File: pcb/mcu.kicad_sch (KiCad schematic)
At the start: 11 parts, among them SW1 TS-1088-AR02016, SW2 TS-1088-AR02016, U1 ESP32-S3-MINI-1

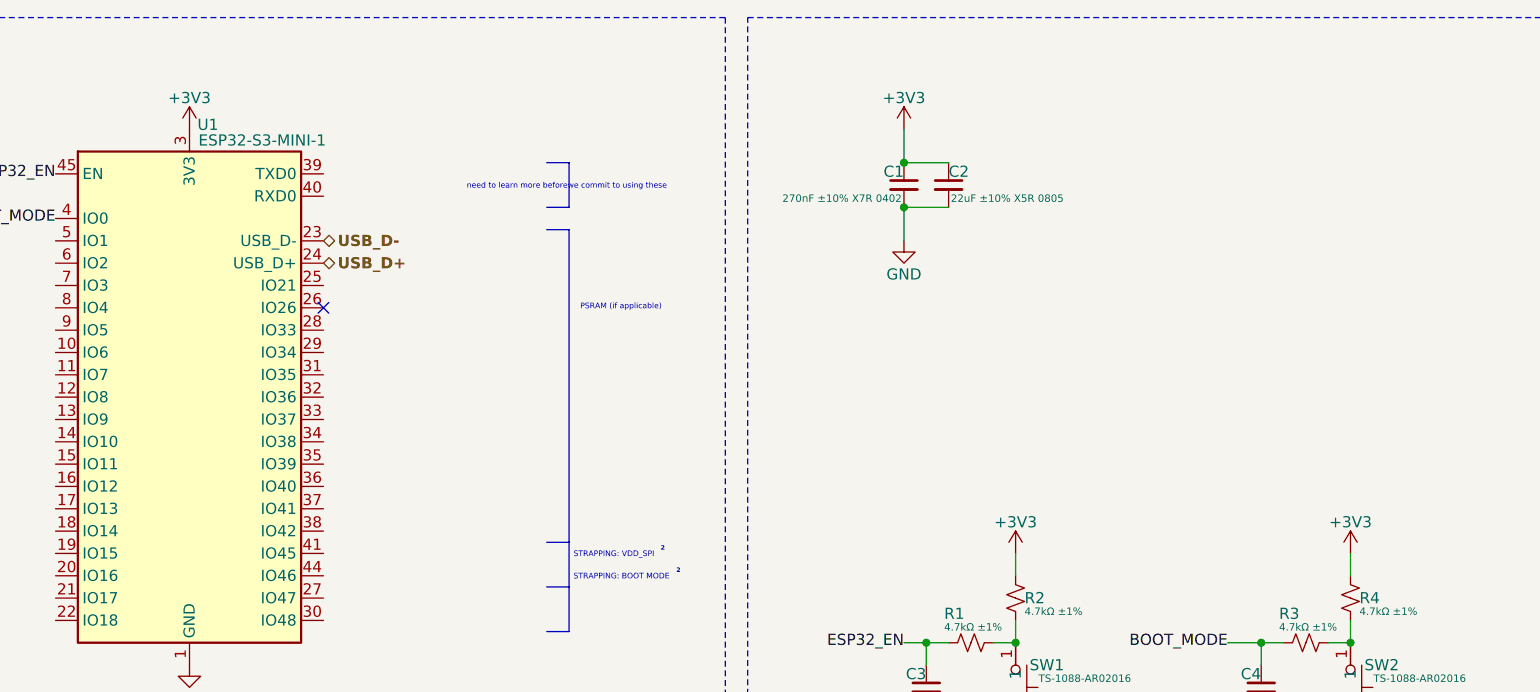
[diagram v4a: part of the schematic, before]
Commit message: Completed Initial Power Draft for Review, and Updated Flags
Included notes for review
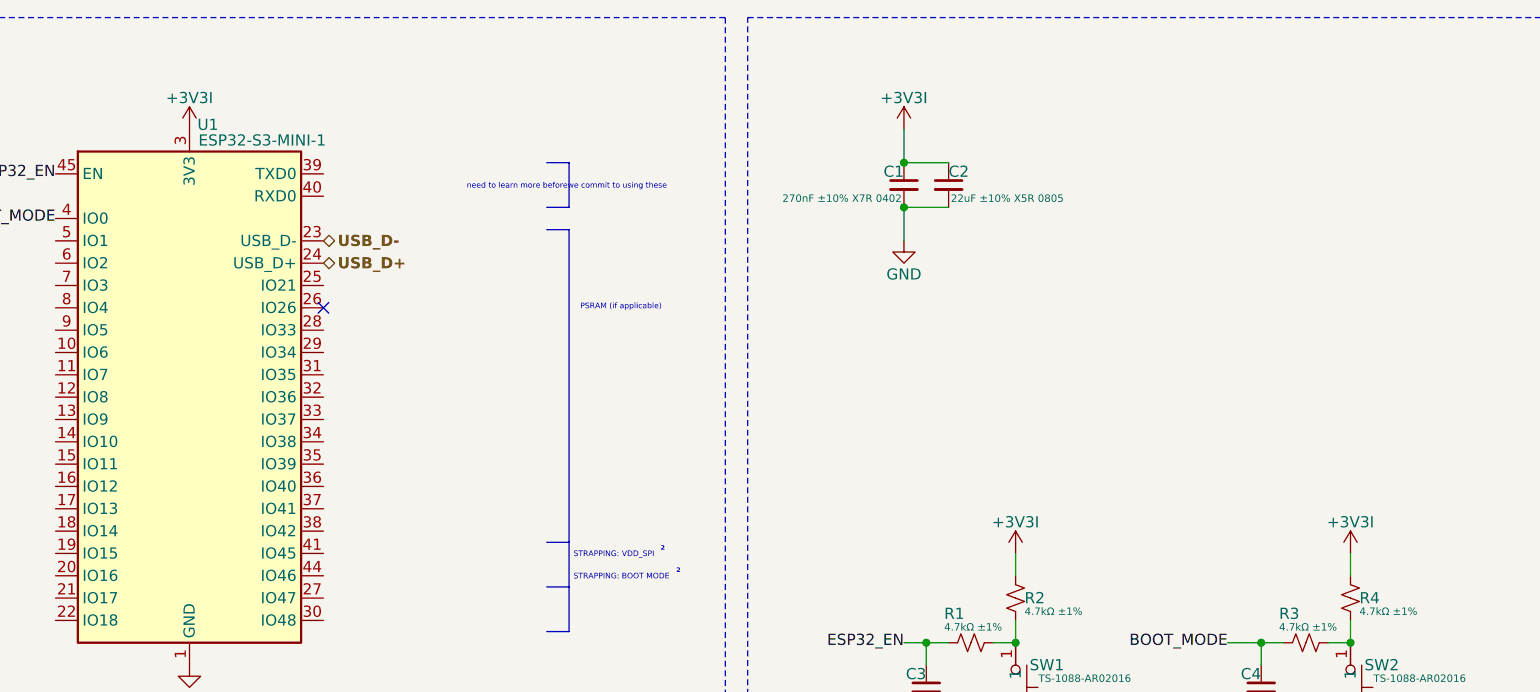
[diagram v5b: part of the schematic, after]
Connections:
- net +3V3 renamed +3V3I
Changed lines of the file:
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@@
 			)
 		)
-		(property "Value" "+3V3"
+		(property "Value" "+3V3I"
 			(at 208.28 70.104 0)
 			(effects
@@
 			)
 		)
-		(property "Value" "+3V3"
+		(property "Value" "+3V3I"
 			(at 246.38 70.104 0)
 			(effects
@@
 			)
 		)
-		(property "Value" "+3V3"
+		(property "Value" "+3V3I"
 			(at 195.58 21.844 0)
 			(effects
@@
 			)
 		)
-		(property "Value" "+3V3"
+		(property "Value" "+3V3I"
 			(at 114.3 21.844 0)
 			(effects

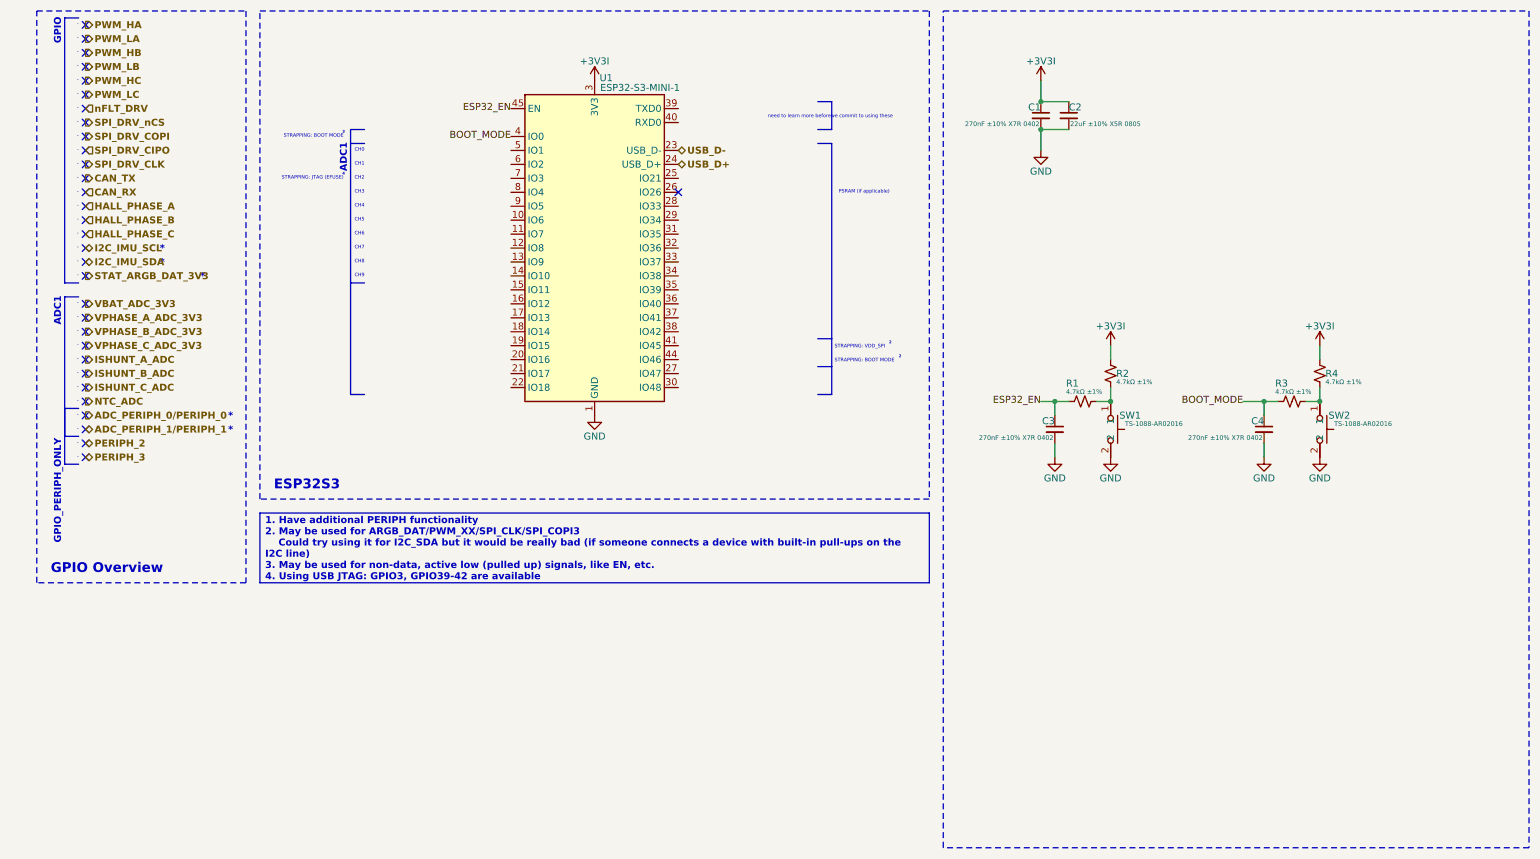
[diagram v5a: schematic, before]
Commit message: Updating label direction, added more info on io
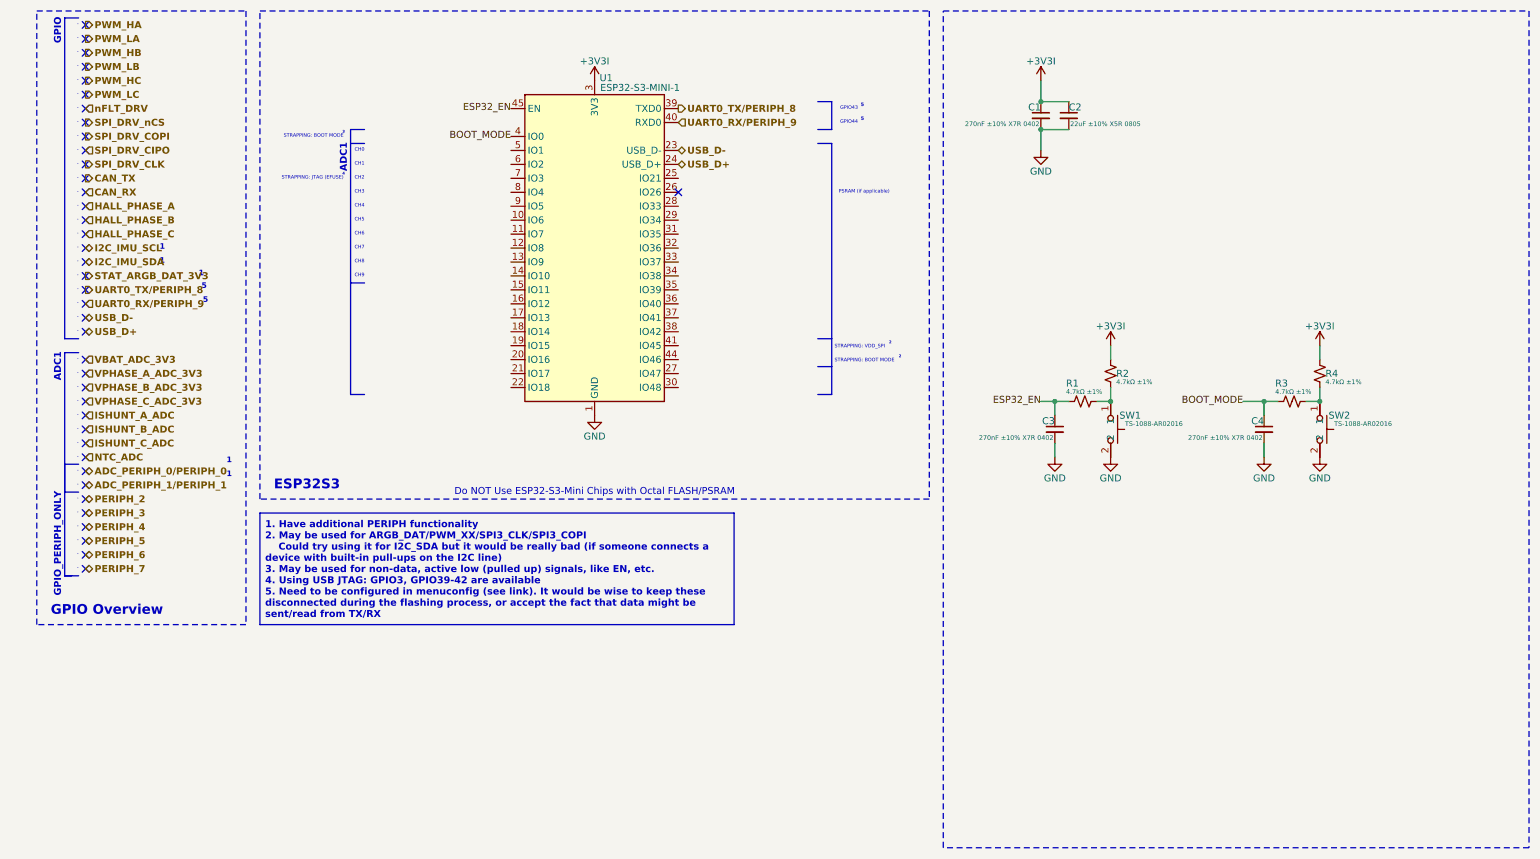
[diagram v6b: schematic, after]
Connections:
- net UART0_TX/PERIPH_8: now reaches U1.39 (TXD0)
- net UART0_RX/PERIPH_9: now reaches U1.40 (RXD0)
- no-connect marks 32 -> 40
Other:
- note added: "5"
- note added: "Do NOT Use ESP32-S3-Mini Chips with Octal FLASH/PSRAM"
- note added: "GPIO43"
- note added: "GPIO44"
- note added: "^{1}"
- note added: "^{5}"
- note removed: "*"
- note removed: "need to learn more beforewe commit to using these"

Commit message: Made updates to the power and driver sheet
Fixed converters and added motor connector
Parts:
- renumbered C2 to C?, C4 to C?, C1 to C?, C3 to C?, R1 to R?, R2 to R?, R3 to R?, R4 to R?, SW2 to SW?, SW1 to SW?, U1 to U?
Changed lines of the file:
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@@
 		(on_board yes)
 		(dnp no)
-		(property "Reference" "#PWR08"
+		(property "Reference" "#PWR?"
 			(at 236.22 100.33 0)
 			(effects
@@
 			(project "sresc"
 				(path "/5072676b-6ffc-4812-9165-a6d5aae17d98/1c391981-fffe-4c54-847d-b61b4420497c"
-					(reference "#PWR08")
+					(reference "#PWR?")
 					(unit 1)
 				)
@@
 		(on_board yes)
 		(dnp no)
-		(property "Reference" "#PWR06"
+		(property "Reference" "#PWR?"
 			(at 208.28 77.47 0)
 			(effects
@@
 			(project "sresc"
 				(path "/5072676b-6ffc-4812-9165-a6d5aae17d98/1c391981-fffe-4c54-847d-b61b4420497c"
-					(reference "#PWR06")
+					(reference "#PWR?")
 					(unit 1)
 				)
@@
 		(on_board yes)
 		(dnp no)
-		(property "Reference" "SW2"
+		(property "Reference" "SW?"
 			(at 249.936 86.36 90)
 			(effects
@@
 			(project "sresc"
 				(path "/5072676b-6ffc-4812-9165-a6d5aae17d98/1c391981-fffe-4c54-847d-b61b4420497c"
-					(reference "SW2")
+					(reference "SW?")
 					(unit 1)
 				)
@@
 		(on_board yes)
 		(dnp no)
-		(property "Reference" "#PWR09"
+		(property "Reference" "#PWR?"
 			(at 246.38 77.47 0)
 			(effects
@@
 			(project "sresc"
 				(path "/5072676b-6ffc-4812-9165-a6d5aae17d98/1c391981-fffe-4c54-847d-b61b4420497c"
-					(reference "#PWR09")
+					(reference "#PWR?")
 					(unit 1)
 				)
@@
 		(on_board yes)
 		(dnp no)
-		(property "Reference" "C2"
+		(property "Reference" "C?"
 			(at 200.66 30.226 0)
 			(effects
@@
 			(project "sresc"
 				(path "/5072676b-6ffc-4812-9165-a6d5aae17d98/1c391981-fffe-4c54-847d-b61b4420497c"
-					(reference "C2")
+					(reference "C?")
 					(unit 1)
 				)
@@
 		(on_board yes)
 		(dnp no)
-		(property "Reference" "SW1"
+		(property "Reference" "SW?"
 			(at 211.836 86.36 90)
 			(effects
@@
 			(project "sresc"
 				(path "/5072676b-6ffc-4812-9165-a6d5aae17d98/1c391981-fffe-4c54-847d-b61b4420497c"
-					(reference "SW1")
+					(reference "SW?")
 					(unit 1)
 				)
@@
 		(on_board yes)
 		(dnp no)
-		(property "Reference" "#PWR04"
+		(property "Reference" "#PWR?"
 			(at 195.58 44.45 0)
 			(effects
@@
 			(project "sresc"
 				(path "/5072676b-6ffc-4812-9165-a6d5aae17d98/1c391981-fffe-4c54-847d-b61b4420497c"
-					(reference "#PWR04")
+					(reference "#PWR?")
 					(unit 1)
 				)
@@
 		(on_board yes)
 		(dnp no)
-		(property "Reference" "#PWR03"
+		(property "Reference" "#PWR?"
 			(at 195.58 29.21 0)
 			(effects
@@
 			(project "sresc"
 				(path "/5072676b-6ffc-4812-9165-a6d5aae17d98/1c391981-fffe-4c54-847d-b61b4420497c"
-					(reference "#PWR03")
+					(reference "#PWR?")
 					(unit 1)
 				)
@@
 		(on_board yes)
 		(dnp no)
-		(property "Reference" "#PWR07"
+		(property "Reference" "#PWR?"
 			(at 208.28 100.33 0)
 			(effects
@@
 			(project "sresc"
 				(path "/5072676b-6ffc-4812-9165-a6d5aae17d98/1c391981-fffe-4c54-847d-b61b4420497c"
-					(reference "#PWR07")
+					(reference "#PWR?")
 					(unit 1)
 				)
@@
 		(on_board yes)
 		(dnp no)
-		(property "Reference" "R1"
+		(property "Reference" "R?"
 			(at 200.152 80.518 90)
 			(effects
@@
 			(project "sresc"
 				(path "/5072676b-6ffc-4812-9165-a6d5aae17d98/1c391981-fffe-4c54-847d-b61b4420497c"
-					(reference "R1")
+					(reference "R?")
 					(unit 1)
 				)
@@
 		(on_board yes)
 		(dnp no)
-		(property "Reference" "C4"
+		(property "Reference" "C?"
 			(at 236.22 87.376 0)
 			(effects
@@
 			(project "sresc"
 				(path "/5072676b-6ffc-4812-9165-a6d5aae17d98/1c391981-fffe-4c54-847d-b61b4420497c"
-					(reference "C4")
+					(reference "C?")
 					(unit 1)
 				)
@@
 		(on_board yes)
 		(dnp no)
-		(property "Reference" "U1"
+		(property "Reference" "U?"
 			(at 115.2047 24.892 0)
 			(effects
@@
 			(project ""
 				(path "/5072676b-6ffc-4812-9165-a6d5aae17d98/1c391981-fffe-4c54-847d-b61b4420497c"
-					(reference "U1")
+					(reference "U?")
 					(unit 1)
 				)
@@
 		(on_board yes)
 		(dnp no)
-		(property "Reference" "R2"
+		(property "Reference" "R?"
 			(at 209.296 78.74 0)
 			(effects
@@
 			(project "sresc"
 				(path "/5072676b-6ffc-4812-9165-a6d5aae17d98/1c391981-fffe-4c54-847d-b61b4420497c"
-					(reference "R2")
+					(reference "R?")
 					(unit 1)
 				)
@@
 		(on_board yes)
 		(dnp no)
-		(property "Reference" "#PWR01"
+		(property "Reference" "#PWR?"
 			(at 114.3 29.21 0)
 			(effects
@@
 			(project ""
 				(path "/5072676b-6ffc-4812-9165-a6d5aae17d98/1c391981-fffe-4c54-847d-b61b4420497c"
-					(reference "#PWR01")
+					(reference "#PWR?")
 					(unit 1)
 				)
@@
 		(on_board yes)
 		(dnp no)
-		(property "Reference" "#PWR010"
+		(property "Reference" "#PWR?"
 			(at 246.38 100.33 0)
 			(effects
@@
 			(project "sresc"
 				(path "/5072676b-6ffc-4812-9165-a6d5aae17d98/1c391981-fffe-4c54-847d-b61b4420497c"
-					(reference "#PWR010")
+					(reference "#PWR?")
 					(unit 1)
 				)
@@
 		(on_board yes)
 		(dnp no)
-		(property "Reference" "#PWR05"
+		(property "Reference" "#PWR?"
 			(at 198.12 100.33 0)
 			(effects
@@
 			(project "sresc"
 				(path "/5072676b-6ffc-4812-9165-a6d5aae17d98/1c391981-fffe-4c54-847d-b61b4420497c"
-					(reference "#PWR05")
+					(reference "#PWR?")
 					(unit 1)
 				)
@@
 		(on_board yes)
 		(dnp no)
-		(property "Reference" "R3"
+		(property "Reference" "R?"
 			(at 238.252 80.518 90)
 			(effects
@@
 			(project "sresc"
 				(path "/5072676b-6ffc-4812-9165-a6d5aae17d98/1c391981-fffe-4c54-847d-b61b4420497c"
-					(reference "R3")
+					(reference "R?")
 					(unit 1)
 				)
@@
 		(on_board yes)
 		(dnp no)
-		(property "Reference" "C1"
+		(property "Reference" "C?"
 			(at 195.58 30.226 0)
 			(effects
@@
 			(project "sresc"
 				(path "/5072676b-6ffc-4812-9165-a6d5aae17d98/1c391981-fffe-4c54-847d-b61b4420497c"
-					(reference "C1")
+					(reference "C?")
 					(unit 1)
 				)
@@
 		(on_board yes)
 		(dnp no)
-		(property "Reference" "#PWR02"
+		(property "Reference" "#PWR?"
 			(at 114.3 92.71 0)
 			(effects
@@
 			(project "sresc"
 				(path "/5072676b-6ffc-4812-9165-a6d5aae17d98/1c391981-fffe-4c54-847d-b61b4420497c"
-					(reference "#PWR02")
+					(reference "#PWR?")
 					(unit 1)
 				)
@@
 		(on_board yes)
 		(dnp no)
-		(property "Reference" "R4"
+		(property "Reference" "R?"
 			(at 247.396 78.74 0)
 			(effects
@@
 			(project "sresc"
 				(path "/5072676b-6ffc-4812-9165-a6d5aae17d98/1c391981-fffe-4c54-847d-b61b4420497c"
-					(reference "R4")
+					(reference "R?")
 					(unit 1)
 				)
@@
 		(on_board yes)
 		(dnp no)
-		(property "Reference" "C3"
+		(property "Reference" "C?"
 			(at 198.12 87.376 0)
 			(effects
@@
 			(project "sresc"
 				(path "/5072676b-6ffc-4812-9165-a6d5aae17d98/1c391981-fffe-4c54-847d-b61b4420497c"
-					(reference "C3")
-					(unit 1)
-				)
+					(reference "C?")
+					(unit 1)
+				)
